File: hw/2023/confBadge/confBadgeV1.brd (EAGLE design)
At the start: 96.5 x 78.7 mm, 84 parts, among them J1 10118192-0002LF, Q1 8/16/20MHz, U1 ATMEGA328, U10 WS2812-2020, U11 WS2812-2020, U12 WS2812-2020, U13 WS2812-2020, U14 WS2812-2020, U15 WS2812-2020, U16 WS2812-2020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

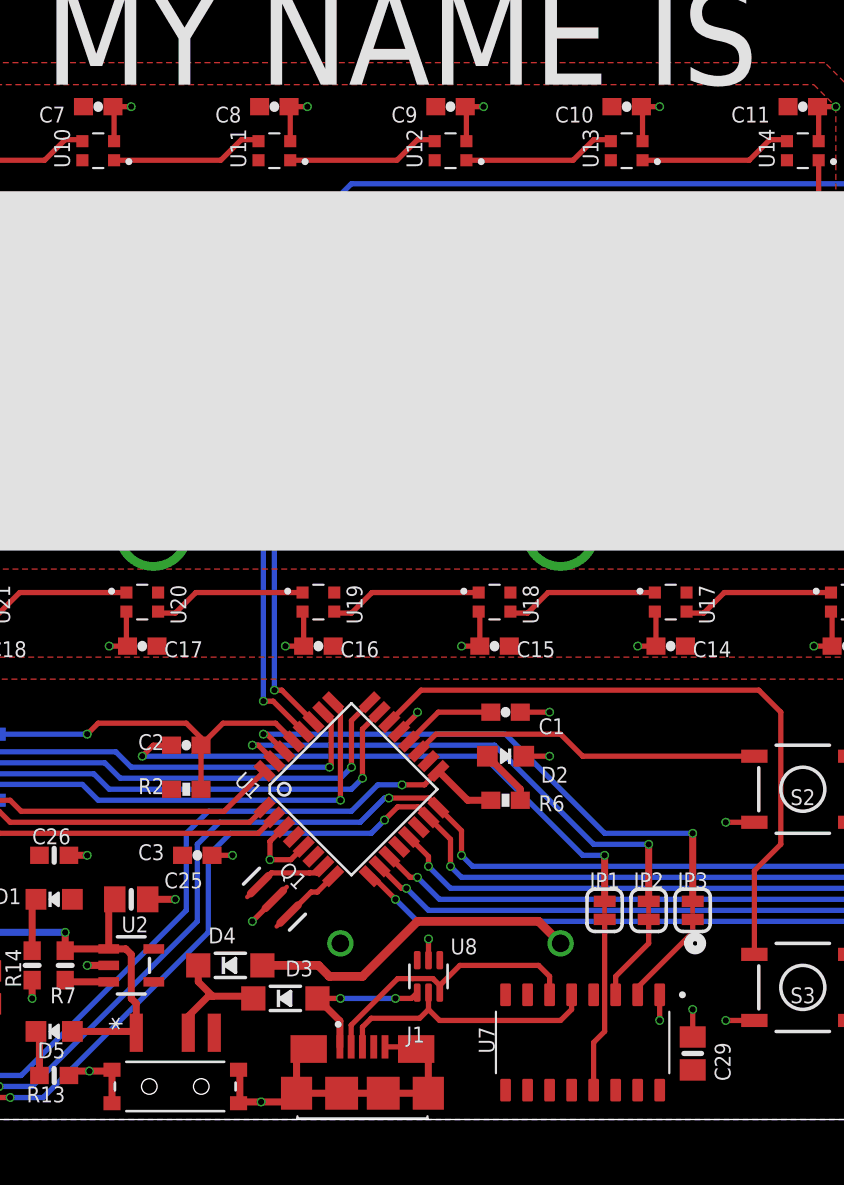
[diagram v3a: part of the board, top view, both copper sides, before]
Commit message: Created gerbers
- changed some footprint to only have 0.1uF at 0603 (removed 0805)
- created gerbers and pick-n-place files for JLCPCB
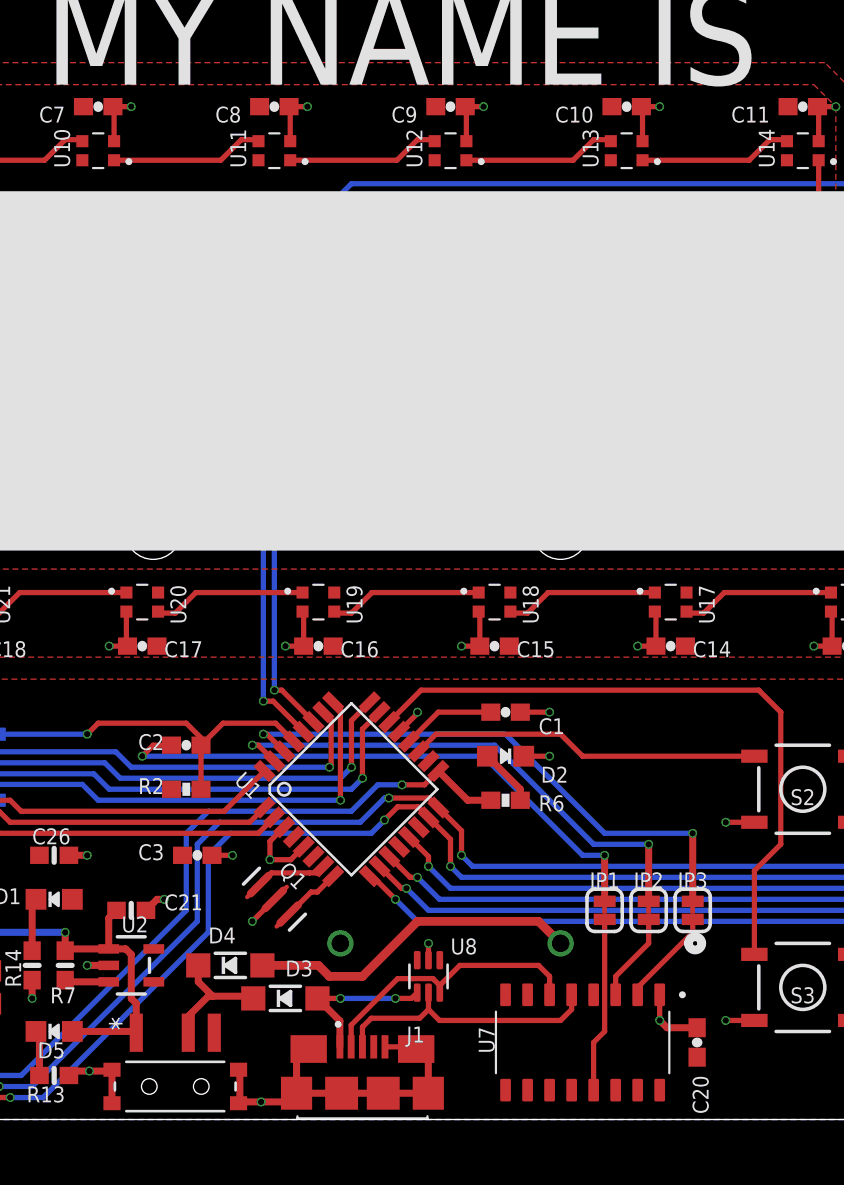
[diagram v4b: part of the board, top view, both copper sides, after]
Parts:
- removed C25: 1uF, microbuilder:0805-NO
- removed C29: 0.1uF, microbuilder:0805-NO
- added C20: 0.1uF, SparkFun:0603-CAP
- added C21: 1uF, microbuilder:0603-NO
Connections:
- net 3.3V: now also C20.2; no longer C29.1
- net GND: now also C20.1, C21.2; no longer C25.2, C29.2
- net VDD: now also C21.1; no longer C25.1
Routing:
- net VDD: track 51.5 -> 50.6 mm
- net GND: track 116.2 -> 116.4 mm, vias 42 -> 41
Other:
- board text added: "RST"
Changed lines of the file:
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@@
 <setting verticaltext="up"/>
 </settings>
-<grid distance="50" unitdist="mil" unit="mil" style="lines" multiple="1" display="yes" altdistance="5" altunitdist="mil" altunit="mil"/>
+<grid distance="25" unitdist="mil" unit="mil" style="lines" multiple="1" display="yes" altdistance="5" altunitdist="mil" altunit="mil"/>
 <layers>
-<layer number="1" name="Top" color="4" fill="1" visible="no" active="yes"/>
-<layer number="16" name="Bottom" color="1" fill="1" visible="no" active="yes"/>
+<layer number="1" name="Top" color="4" fill="1" visible="yes" active="yes"/>
+<layer number="16" name="Bottom" color="1" fill="1" visible="yes" active="yes"/>
 <layer number="17" name="Pads" color="2" fill="1" visible="yes" active="yes"/>
 <layer number="18" name="Vias" color="2" fill="1" visible="yes" active="yes"/>
 <layer number="19" name="Unrouted" color="6" fill="1" visible="yes" active="yes"/>
 <layer number="20" name="Dimension" color="24" fill="1" visible="yes" active="yes"/>
-<layer number="21" name="tPlace" color="7" fill="1" visible="no" active="yes"/>
-<layer number="22" name="bPlace" color="7" fill="1" visible="yes" active="yes"/>
-<layer number="23" name="tOrigins" color="15" fill="1" visible="no" active="yes"/>
+<layer number="21" name="tPlace" color="7" fill="1" visible="yes" active="yes"/>
+<layer number="22" name="bPlace" color="7" fill="1" visible="no" active="yes"/>
+<layer number="23" name="tOrigins" color="15" fill="1" visible="yes" active="yes"/>
 <layer number="24" name="bOrigins" color="15" fill="1" visible="no" active="yes"/>
 <layer number="25" name="tNames" color="7" fill="1" visible="no" active="yes"/>
-<layer number="26" name="bNames" color="7" fill="1" visible="yes" active="yes"/>
+<layer number="26" name="bNames" color="7" fill="1" visible="no" active="yes"/>
 <layer number="27" name="tValues" color="7" fill="1" visible="no" active="yes"/>
 <layer number="28" name="bValues" color="7" fill="1" visible="no" active="yes"/>
@@
 <layer number="120" name="KAP_MAAT1" color="7" fill="1" visible="yes" active="yes"/>
 <layer number="121" name="_tsilk" color="29" fill="1" visible="yes" active="yes"/>
-<layer number="122" name="_bsilk" color="21" fill="1" visible="no" active="yes"/>
+<layer number="122" name="_bsilk" color="21" fill="1" visible="yes" active="yes"/>
 <layer number="123" name="tTestmark" color="7" fill="1" visible="no" active="yes"/>
 <layer number="124" name="bTestmark" color="7" fill="1" visible="no" active="yes"/>
@@
 2023.PROTO1</text>
 <text x="1.27" y="7.112" size="1.27" layer="21" rot="R45">ISP</text>
+<text x="25.4" y="23.114" size="0.9144" layer="22" rot="MR0">RST</text>
 </plain>
 <attributes>
@@
 <attribute name="VALUE" x="39.116" y="22.733" size="0.4064" layer="27" font="vector" rot="R180"/>
 </element>
-<element name="C25" library="microbuilder" package="0805-NO" value="1uF" x="34.925" y="12.7" smashed="yes">
-<attribute name="NAME" x="36.83" y="13.335" size="0.9144" layer="25" ratio="18"/>
-<attribute name="VALUE" x="36.957" y="11.938" size="0.4064" layer="27" ratio="10"/>
-</element>
 <element name="C26" library="microbuilder" package="0603-NO" value="1uF" x="30.48" y="15.24" smashed="yes">
 <attribute name="NAME" x="29.21" y="15.875" size="0.9144" layer="25" ratio="18"/>
@@
 <attribute name="VALUE" x="27.432" y="9.652" size="0.4064" layer="27" ratio="10" rot="R90"/>
 </element>
-<element name="C29" library="microbuilder" package="0805-NO" value="0.1uF" x="67.31" y="3.81" smashed="yes" rot="R90">
-<attribute name="NAME" x="68.58" y="4.445" size="0.9144" layer="25" ratio="18" rot="R270"/>
-<attribute name="VALUE" x="68.072" y="5.842" size="0.4064" layer="27" ratio="10" rot="R90"/>
-</element>
 <element name="C3" library="SparkFun" package="0603-CAP" value="0.1uF" x="38.735" y="15.24" smashed="yes" rot="R180">
 <attribute name="NAME" x="36.83" y="15.875" size="0.9144" layer="25" rot="R180"/>
@@
 <attribute name="VALUE" x="8.3065125" y="6.51045625" size="1.27" layer="27" ratio="10" rot="R135"/>
 </element>
+<element name="C20" library="SparkFun" package="0603-CAP" value="0.1uF" x="67.564" y="4.445" smashed="yes" rot="R270">
+<attribute name="NAME" x="67.31" y="2.54" size="0.9144" layer="25" rot="R270"/>
+<attribute name="VALUE" x="66.421" y="5.461" size="0.4064" layer="27" font="vector" rot="R270"/>
+</element>
+<element name="C21" library="microbuilder" package="0603-NO" value="1uF" x="34.925" y="12.065" smashed="yes">
+<attribute name="NAME" x="36.83" y="12.065" size="0.9144" layer="25" ratio="18"/>
+<attribute name="VALUE" x="36.703" y="11.303" size="0.4064" layer="27" font="vector" ratio="10"/>
+</element>
 </elements>
 <signals>
@@
 <contactref element="U1" pad="21"/>
 <contactref element="C26" pad="2"/>
-<contactref element="C25" pad="2"/>
 <contactref element="C27" pad="2"/>
 <contactref element="U2" pad="2"/>
@@
 <contactref element="J1" pad="S6"/>
 <contactref element="J1" pad="5"/>
-<contactref element="C29" pad="2"/>
 <contactref element="U7" pad="1"/>
 <contactref element="U8" pad="2"/>
@@
 <wire x1="31.33" y1="15.24" x2="32.385" y2="15.24" width="0.4064" layer="1"/>
 <via x="32.385" y="15.24" extent="1-16" drill="0.35"/>
-<wire x1="35.875" y1="12.7" x2="37.465" y2="12.7" width="0.4064" layer="1"/>
-<via x="37.465" y="12.7" extent="1-16" drill="0.35"/>
-<wire x1="52.07" y1="9.19" x2="52.07" y2="10.414" width="0.3048" layer="1"/>
-<wire x1="52.07" y1="10.414" x2="52.07" y2="10.4225" width="0.3048" layer="1"/>
-<via x="52.07" y="10.414" extent="1-16" drill="0.35"/>
 <wire x1="70.866" y1="5.715" x2="69.215" y2="5.715" width="0.3048" layer="1"/>
 <via x="69.215" y="5.715" extent="1-16" drill="0.35"/>
@@
 <wire x1="51.435" y1="23.4256875" x2="51.435" y2="23.495" width="0.3048" layer="1"/>
 <via x="51.435" y="23.495" extent="1-16" drill="0.35"/>
-<wire x1="67.31" y1="4.76" x2="67.31" y2="6.35" width="0.3048" layer="1"/>
-<via x="67.31" y="6.35" extent="1-16" drill="0.35"/>
 <wire x1="26.67" y1="8.57" x2="26.67" y2="10.16" width="0.3048" layer="1"/>
 <via x="26.67" y="10.16" extent="1-16" drill="0.35"/>
@@
 <wire x1="51.235" y1="4.191" x2="51.36" y2="4.066" width="0.3048" layer="1"/>
 <contactref element="SV5" pad="6"/>
+<contactref element="C20" pad="1"/>
+<contactref element="C21" pad="2"/>
+<wire x1="35.775" y1="12.065" x2="36.41" y2="12.7" width="0.4064" layer="1"/>
+<wire x1="36.41" y1="12.7" x2="36.83" y2="12.7" width="0.4064" layer="1"/>
+<via x="36.83" y="12.7" extent="1-16" drill="0.35"/>
+<wire x1="67.564" y1="5.295" x2="65.825" y2="5.295" width="0.4064" layer="1"/>
+<wire x1="65.825" y1="5.295" x2="65.405" y2="5.715" width="0.4064" layer="1"/>
+<wire x1="52.07" y1="9.19" x2="52.07" y2="10.16" width="0.3048" layer="1"/>
+<via x="52.07" y="10.16" extent="1-16" drill="0.35"/>
 </signal>
 <signal name="AREF">
@@
 <contactref element="U2" pad="5"/>
 <contactref element="D1" pad="A"/>
-<contactref element="C29" pad="1"/>
 <contactref element="U7" pad="16"/>
 <contactref element="U7" pad="4"/>
@@
 <contactref element="R12" pad="1"/>
 <contactref element="SV5" pad="2"/>
+<contactref element="C20" pad="2"/>
 </signal>
 <signal name="EN">
@@
 </signal>
 <signal name="VDD">
-<contactref element="C25" pad="1"/>
 <contactref element="R7" pad="2"/>
 <contactref element="U5" pad="1"/>
@@
 <contactref element="C17" pad="2"/>
 <contactref element="C18" pad="2"/>
-<wire x1="33.6249" y1="9.84" x2="33.6249" y2="12.3499" width="0.4064" layer="1"/>
-<wire x1="33.6249" y1="12.3499" x2="33.975" y2="12.7" width="0.4064" layer="1"/>
 <wire x1="33.6249" y1="9.84" x2="31.215" y2="9.84" width="0.4064" layer="1"/>
 <wire x1="31.215" y1="9.84" x2="31.115" y2="9.74" width="0.4064" layer="1"/>
@@
 <vertex x="0" y="53.34"/>
 </polygon>
-<wire x1="62.65" y1="58.42" x2="62.90486875" y2="58.42" width="0.3048" layer="1"/>
 <wire x1="31.115" y1="9.74" x2="31.115" y2="10.795" width="0.4064" layer="1"/>
 <via x="31.115" y="10.795" extent="1-16" drill="0.35"/>
@@
 <wire x1="12.065" y1="12.065" x2="12.065" y2="27.305" width="0.4064" layer="16"/>
 <via x="12.065" y="27.305" extent="1-16" drill="0.35"/>
+<contactref element="C21" pad="1"/>
+<wire x1="34.075" y1="12.065" x2="33.6249" y2="11.6149" width="0.4064" layer="1"/>
+<wire x1="33.6249" y1="11.6149" x2="33.6249" y2="9.84" width="0.4064" layer="1"/>
 </signal>
 <signal name="N$34">

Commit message: Switch to USB-C for both badge
ctf-badge
- switched to USB-C
- switched to smaller neopixel
- switched to 3xAAA
- removed lipo charging circuit
conf-badge
- switched to USB-C
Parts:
- removed J1: 10118192-0002LF, 10118192-0002LF:AMPHENOL_10118192-0002LF
- added J3: TYPE-C-31-M-12, TYPE-C-31-M-12:HRO_TYPE-C-31-M-12
- added R1, R5: 5.1K, microbuilder:0603-NO
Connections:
- removed net N$28: J1.3, U7.5, U8.5
- removed net N$29: J1.2, U7.6, U8.6
- new net N$27: J3.B5, R5.1
- new net N$30: J3.A5, R1.1
- new net USB_DN: J3.A7, J3.B7, U7.6, U8.6
- new net USB_DP: J3.A6, J3.B6, U7.5, U8.5
- net GND: now also J3.A1/B12, J3.B1/A12, J3.S1, J3.S2, J3.S3, J3.S4, R1.2, R5.2; no longer J1.5, J1.S1, J1.S2, J1.S3, J1.S4, J1.S5, J1.S6
- net VBUS: now also J3.A4/B9, J3.B4/A9; no longer J1.1
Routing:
- net N$29: track 16.2 -> 0.00 mm
- net N$28: track 16.0 -> 0.00 mm
- net GND: track 116.4 -> 100.6 mm
- net USB_DN: track 0.00 -> 14.9 mm
- net USB_DP: track 0.00 -> 14.8 mm
- net VBUS: track 9.22 -> 7.73 mm

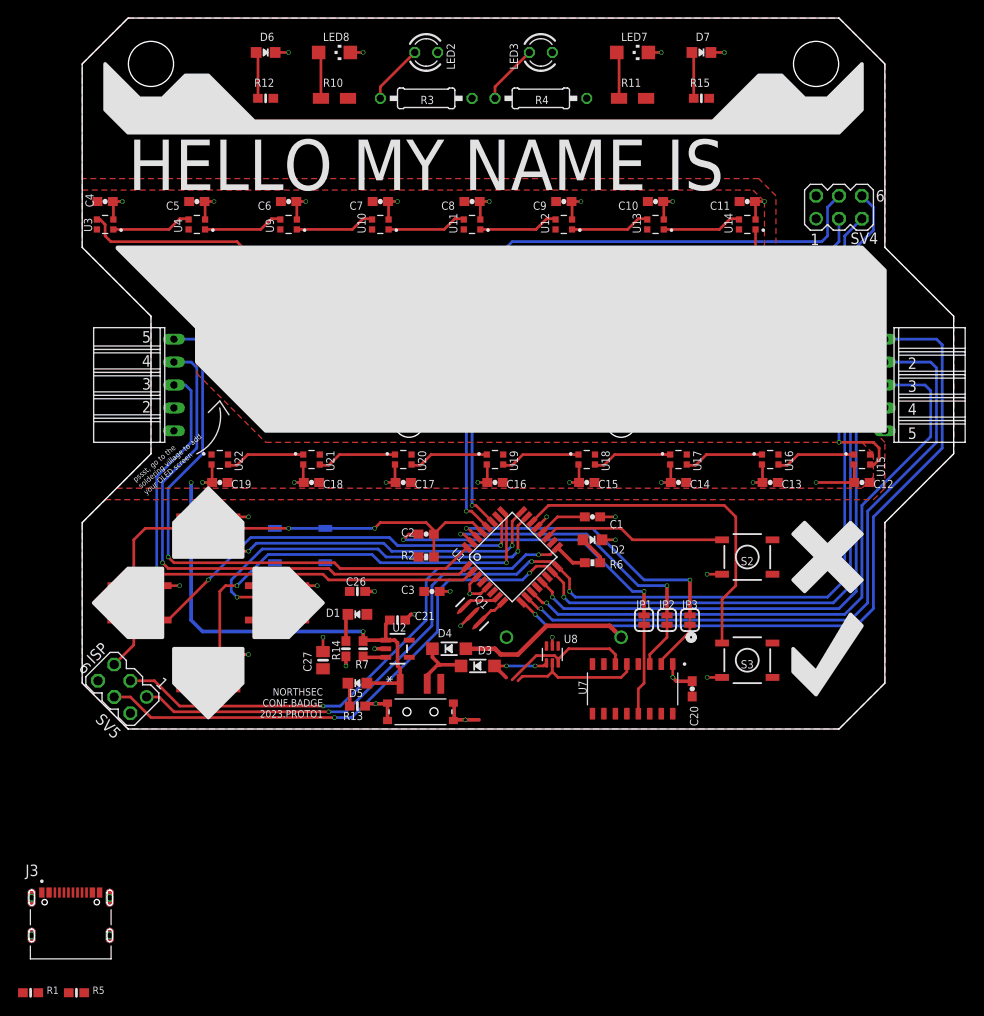
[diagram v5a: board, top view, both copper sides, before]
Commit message: Updated schematic and layout for Conf-Badge
- adjusted for ATmega328PB
- change to USB-c
- switch sao and isp header to SMD
- moved sync-in and sync-out header for fit
- updated silkscreen for oled position
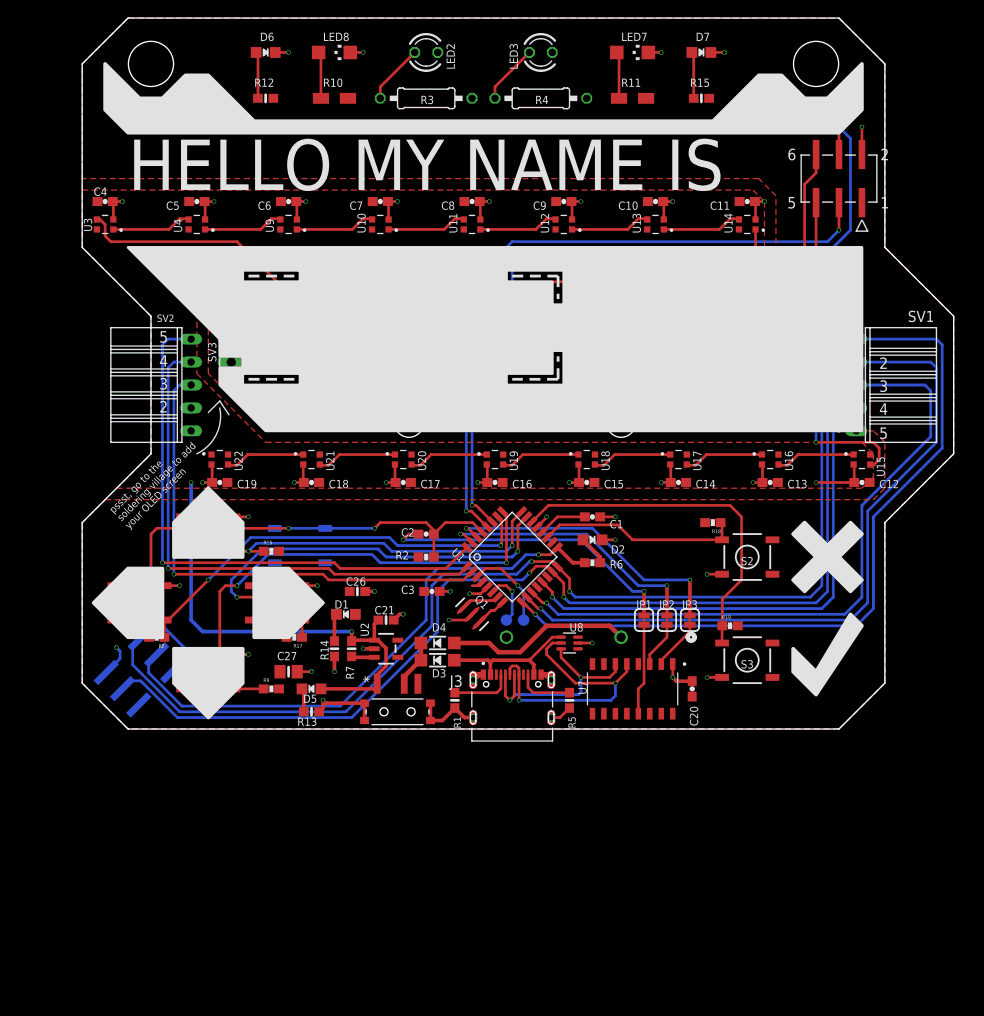
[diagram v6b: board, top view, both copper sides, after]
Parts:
- removed SV4: SAO, con-lstb:MA03-2
- removed SV5: ICSP, con-lstb:MA03-2
- added J1, J2: SSW-103-22-F-D-VS-K-TRCON3_SSW-D-DUMZ_HDR_SAI, SSW-103-22-F-D-VS-K-TR:CON3_SSW-D-DUMZ_HDR_SAI
- added R16, R17, R18, R19, R8, R9: 10K, SparkFun:0603-RES
- added TP1, TP2: TPB1,27, testpad:B1,27
- R13, R14: value 1K -> 5.1K
- moved R5 63.5 mm to (54.0, 3.17), turned to 270 degrees
- moved R1 57.1 mm to (41.3, 3.17), turned to 270 degrees
- moved J3 54.5 mm to (47.6, 1.27)
- moved D5 5.12 mm to (25.4, 4.45)
- moved R13 5.12 mm to (25.4, 1.91)
- moved D3 4.49 mm to (39.4, 7.62)
- moved C27 4.02 mm to (22.9, 6.35), turned to 0 degrees
- moved SV1 3.18 mm to (85.7, 38.1)
- moved U5 2.54 mm to (34.9, 1.91)
- moved U8 2.29 mm to (54.0, 9.53), turned to 180 degrees
- moved SV2 1.90 mm to (12.1, 38.1)
- moved D4 1.42 mm to (39.4, 9.53)
- moved D1 1.27 mm to (29.2, 12.7)
- moved R14 1.27 mm to (27.9, 8.89)
- moved R7 1.27 mm to (29.8, 8.89)
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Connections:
- new net PE0: TP2.TP, U1.3
- new net PE1: TP1.TP, U1.6
- net 3.3V: now also J1.6, J2.1, R16.2, R17.2, R18.2, R19.2, R8.2, R9.2; no longer SV4.2, SV5.2, U1.6
- net BTN_A: now also R19.1
- net BTN_B: now also R18.1
- net BTN_D: now also R9.1
- net BTN_L: now also R8.1
- net BTN_R: now also R17.1
- net BTN_U: now also R16.1
- net DBG_LED: now also J1.3; no longer SV5.3
- net GND: now also J1.2, J2.2; no longer SV4.1, SV5.6, U1.3
- net RESET: now also J1.1; no longer SV5.5
- net SAO_IO1: now also J1.4, J2.5; no longer SV4.6, SV5.4
- net SAO_IO2: now also J1.5, J2.6; no longer SV4.5, SV5.1
- net SCL: now also J2.4; no longer SV4.3
- net SDA: now also J2.3; no longer SV4.4
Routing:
- net USB_DP: track 14.8 -> 31.8 mm, vias 0 -> 2
- net GND: track 100.6 -> 115.4 mm
- net SCL: track 102.3 -> 116.5 mm, vias 3 -> 4
- net SAO_IO2: track 131.5 -> 143.3 mm
- net USB_DN: track 14.9 -> 25.0 mm, vias 0 -> 2
- net PE0: track 0.00 -> 9.76 mm, vias 0 -> 1
- net VBUS: track 7.73 -> 16.2 mm, vias 2 -> 0
- net N$30: track 0.00 -> 6.84 mm
- net N$27: track 0.00 -> 6.26 mm
- net PE1: track 0.00 -> 6.18 mm, vias 0 -> 1
- net 3.3V: track 0.00 -> 4.85 mm, vias 0 -> 1
- net NEOPIX: track 159.1 -> 154.4 mm
- net SAO_IO1: track 140.2 -> 136.4 mm
- net BTN_D: track 51.6 -> 54.9 mm
- net SIG_OUT3: track 69.7 -> 72.9 mm
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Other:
- board text added: "NORTHSEC CONF.BADGE 2023.PROTO2"
- board text added: "SV1"
- board text added: "SV2"
- board text removed: "NORTHSEC CONF.BADGE 2023.PROTO1"
